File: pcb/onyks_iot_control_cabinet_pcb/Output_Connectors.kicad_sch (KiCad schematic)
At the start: 2 parts, among them J5 Conn_02x09_Odd_Even, J6 Conn_01x06_Socket

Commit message: Quick Fixes
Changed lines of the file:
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@@
 			(font
 				(size 3.81 3.81)
-				(thickness 0.762)
-				(bold yes)
+				(thickness 0.4763)
 			)
 		)
@@
 			(font
 				(size 3.81 3.81)
-				(thickness 0.762)
-				(bold yes)
+				(thickness 0.4763)
 			)
 		)

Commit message: Quick fixes
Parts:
- renumbered J5 to J8, J6 to J9
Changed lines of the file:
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@@
 		(dnp no)
 		(fields_autoplaced yes)
-		(property "Reference" "J6"
+		(property "Reference" "J9"
 			(at 163.83 76.2001 0)
 			(effects
@@
 			(project "onyks_iot_control_cabinet_pcb"
 				(path "/789878cb-67d5-4bc7-a42d-b3bc72d661d0/9fa608f4-5282-4caa-ae1b-46582b97cb5d"
-					(reference "J6")
+					(reference "J9")
 					(unit 1)
 				)
@@
 		(on_board yes)
 		(dnp no)
-		(property "Reference" "#PWR025"
+		(property "Reference" "#PWR033"
 			(at 149.86 72.39 0)
 			(effects
@@
 			(project "onyks_iot_control_cabinet_pcb"
 				(path "/789878cb-67d5-4bc7-a42d-b3bc72d661d0/9fa608f4-5282-4caa-ae1b-46582b97cb5d"
-					(reference "#PWR025")
+					(reference "#PWR033")
 					(unit 1)
 				)
@@
 		(dnp no)
 		(fields_autoplaced yes)
-		(property "Reference" "J5"
+		(property "Reference" "J8"
 			(at 153.67 104.14 0)
 			(effects
@@
 			(project "onyks_iot_control_cabinet_pcb"
 				(path "/789878cb-67d5-4bc7-a42d-b3bc72d661d0/9fa608f4-5282-4caa-ae1b-46582b97cb5d"
-					(reference "J5")
+					(reference "J8")
 					(unit 1)
 				)
@@
 		(dnp no)
 		(fields_autoplaced yes)
-		(property "Reference" "#PWR027"
+		(property "Reference" "#PWR035"
 			(at 162.56 139.7 0)
 			(effects
@@
 			(project "onyks_iot_control_cabinet_pcb"
 				(path "/789878cb-67d5-4bc7-a42d-b3bc72d661d0/9fa608f4-5282-4caa-ae1b-46582b97cb5d"
-					(reference "#PWR027")
+					(reference "#PWR035")
 					(unit 1)
 				)
@@
 		(on_board yes)
 		(dnp no)
-		(property "Reference" "#PWR026"
+		(property "Reference" "#PWR034"
 			(at 146.05 73.66 0)
 			(effects
@@
 			(project "onyks_iot_control_cabinet_pcb"
 				(path "/789878cb-67d5-4bc7-a42d-b3bc72d661d0/9fa608f4-5282-4caa-ae1b-46582b97cb5d"
-					(reference "#PWR026")
-					(unit 1)
-				)
+					(reference "#PWR034")
+					(unit 1)
+				)

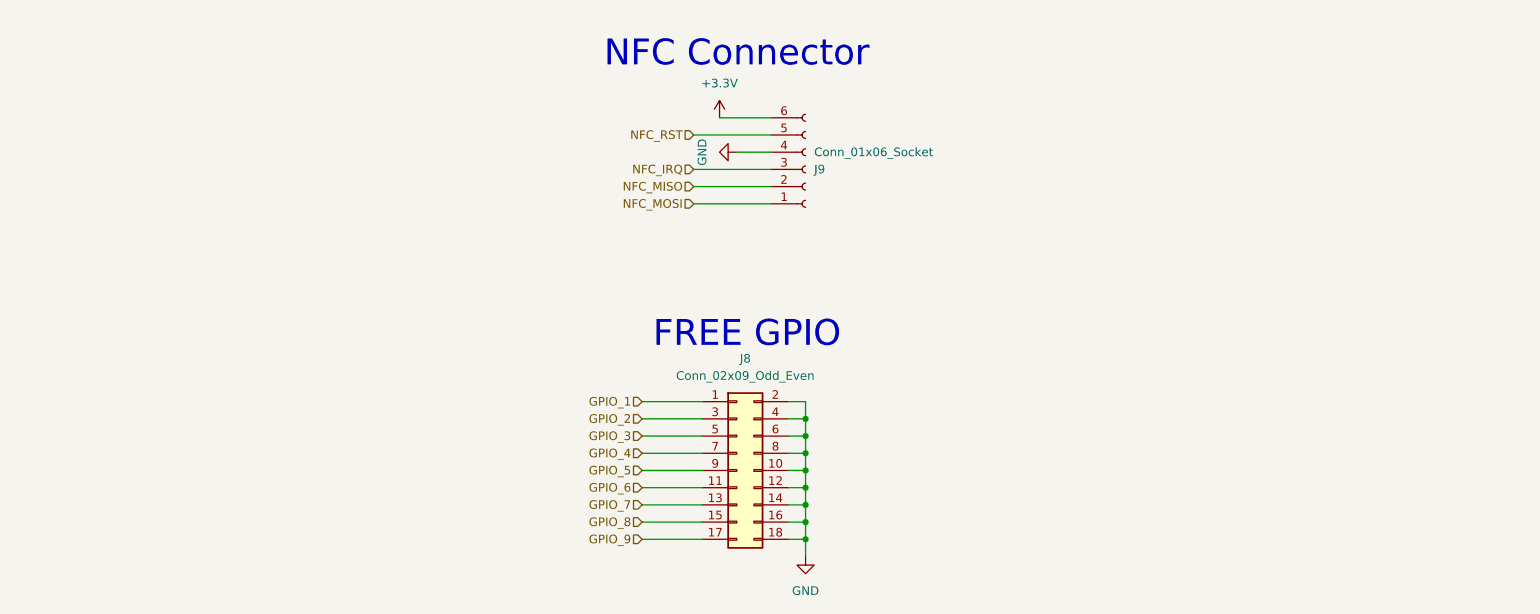
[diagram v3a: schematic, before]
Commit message: Update of the power supply and added the header for 125kHz RFID
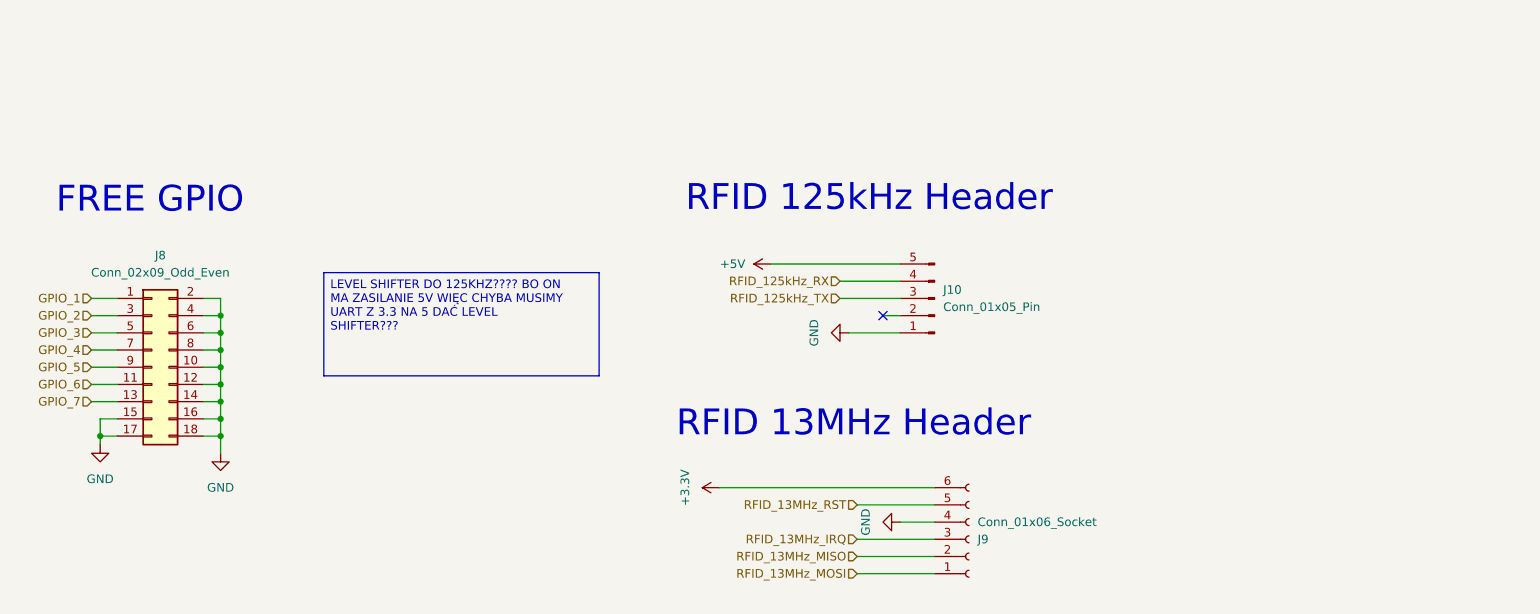
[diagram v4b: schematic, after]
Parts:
- added J10: Conn_01x05_Pin, symbol Connector:Conn_01x05_Pin
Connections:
- net GPIO_8 is gone; now on net GND: J8.15 (Pin_15)
- net GPIO_9 is gone; now on net GND: J8.17 (Pin_17)
- net GND: now also J10.1 (Pin_1)
- net NFC_IRQ renamed RFID_13MHz_IRQ
- net NFC_MISO renamed RFID_13MHz_MISO
- net NFC_MOSI renamed RFID_13MHz_MOSI
- net NFC_RST renamed RFID_13MHz_RST
- new net +5V: J10.5 (Pin_5)
- new net RFID_125kHz_RX: J10.4 (Pin_4)
- new net RFID_125kHz_TX: J10.3 (Pin_3)
- no-connect marks 0 -> 1
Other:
- note added: "RFID 125kHz Header"
- note added: "RFID 13MHz Header"
- note removed: "NFC Connector"
- company: (none) -> ,,Onyks'' Students Scientific Association
- title: (none) -> Onyks Iot Control Cabinet
- moved on the sheet: J8, J9

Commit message: Logic Shifter for RFID 125 KHz
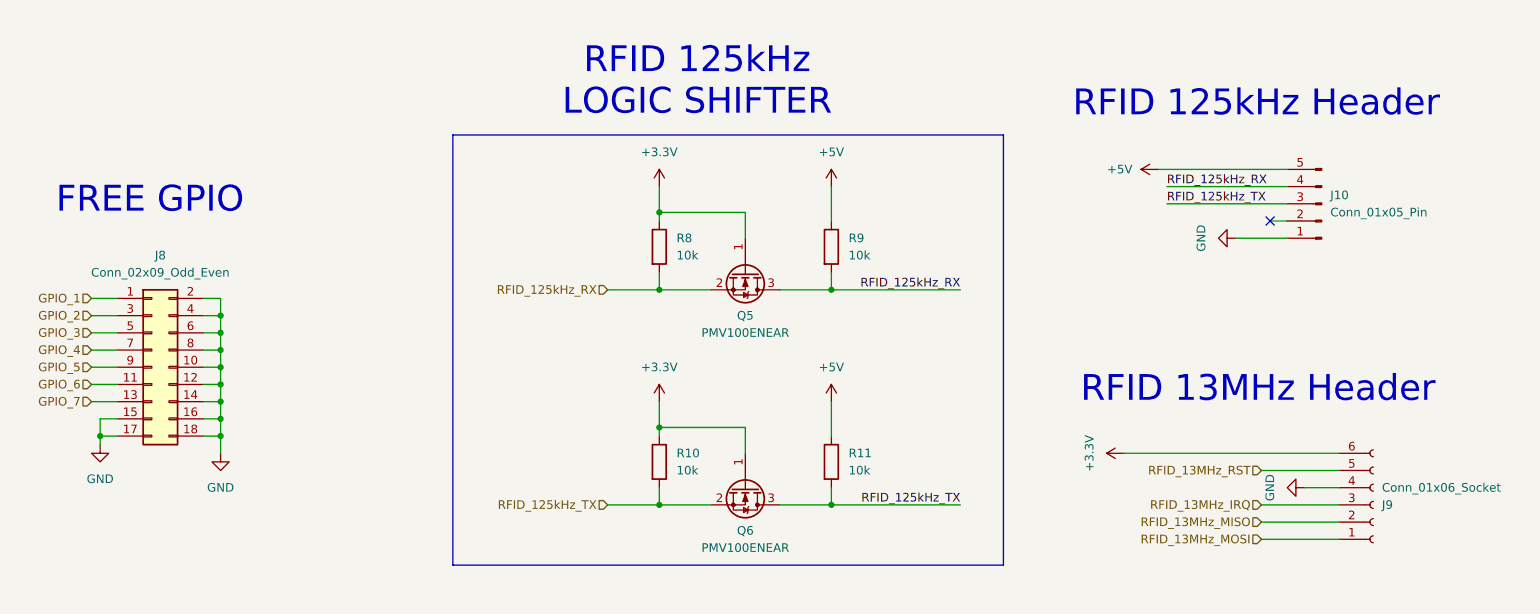
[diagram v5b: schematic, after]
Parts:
- added Q5, Q6: PMV100ENEAR, Package_TO_SOT_SMD:SOT-23, symbol Transistor_FET:2N7002
- added R10, R11, R8, R9: 10k, Resistor_SMD:R_0805_2012Metric_Pad1.20x1.40mm_HandSolder, symbol Device:R
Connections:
- net +3.3V: now also Q5.1 (G), Q6.1 (G), R10.1, R8.1
- net +5V: now also R11.1, R9.1
- net RFID_125kHz_RX: now also Q5.2 (S), Q5.3 (D), R8.2, R9.2
- net RFID_125kHz_TX: now also Q6.2 (S), Q6.3 (D), R10.2, R11.2
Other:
- note added: "RFID 125kHz LOGIC SHIFTER"
- moved on the sheet: J10, J9

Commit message: Schematics update; power supply and footprints fixes
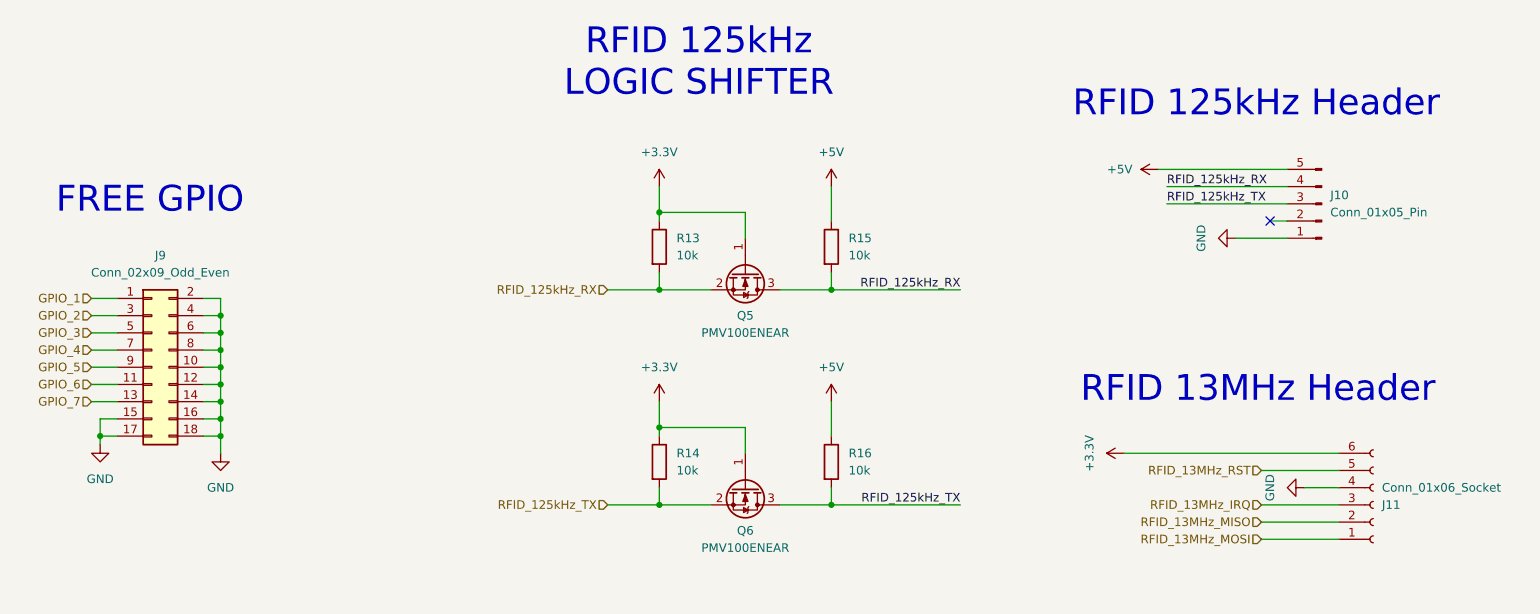
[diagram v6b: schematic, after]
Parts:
- J10: footprint (none) -> Connector_PinHeader_2.54mm:PinHeader_1x05_P2.54mm_Vertical
- renumbered J9 to J11, J8 to J9, R8 to R13, R10 to R14, R9 to R15, R11 to R16
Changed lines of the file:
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@@
 		(comment 2 "Jakub Jastrzębski")
 	)
-	(rectangle
-		(start 110.49 71.12)
-		(end 191.77 134.62)
-		(stroke
-			(width 0)
-			(type default)
-		)
-		(fill
-			(type none)
-		)
-	)
 	(text "RFID 125kHz \nLOGIC SHIFTER"
 		(exclude_from_sim no)
-		(at 146.558 63.246 0)
+		(at 146.812 60.452 0)
 		(effects
 			(font
@@
 		(dnp no)
 		(fields_autoplaced yes)
-		(property "Reference" "J9"
+		(property "Reference" "J11"
 			(at 247.65 125.7301 0)
 			(effects
@@
 			(project "onyks_iot_control_cabinet_pcb"
 				(path "/789878cb-67d5-4bc7-a42d-b3bc72d661d0/9fa608f4-5282-4caa-ae1b-46582b97cb5d"
-					(reference "J9")
+					(reference "J11")
 					(unit 1)
 				)
@@
 		(on_board yes)
 		(dnp no)
-		(property "Reference" "#PWR044"
+		(property "Reference" "#PWR050"
 			(at 140.97 114.3 0)
 			(effects
@@
 			(project "onyks_iot_control_cabinet_pcb"
 				(path "/789878cb-67d5-4bc7-a42d-b3bc72d661d0/9fa608f4-5282-4caa-ae1b-46582b97cb5d"
-					(reference "#PWR044")
+					(reference "#PWR050")
 					(unit 1)
 				)
@@
 		(dnp no)
 		(fields_autoplaced yes)
-		(property "Reference" "#PWR036"
+		(property "Reference" "#PWR051"
 			(at 166.37 82.55 0)
 			(effects
@@
 			(project "onyks_iot_control_cabinet_pcb"
 				(path "/789878cb-67d5-4bc7-a42d-b3bc72d661d0/9fa608f4-5282-4caa-ae1b-46582b97cb5d"
-					(reference "#PWR036")
+					(reference "#PWR051")
 					(unit 1)
 				)
@@
 		(on_board yes)
 		(dnp no)
-		(property "Reference" "#PWR033"
+		(property "Reference" "#PWR053"
 			(at 213.36 118.11 0)
 			(effects
@@
 			(project "onyks_iot_control_cabinet_pcb"
 				(path "/789878cb-67d5-4bc7-a42d-b3bc72d661d0/9fa608f4-5282-4caa-ae1b-46582b97cb5d"
-					(reference "#PWR033")
+					(reference "#PWR053")
 					(unit 1)
 				)
@@
 		(dnp no)
 		(fields_autoplaced yes)
-		(property "Reference" "#PWR045"
+		(property "Reference" "#PWR052"
 			(at 166.37 114.3 0)
 			(effects
@@
 			(project "onyks_iot_control_cabinet_pcb"
 				(path "/789878cb-67d5-4bc7-a42d-b3bc72d661d0/9fa608f4-5282-4caa-ae1b-46582b97cb5d"
-					(reference "#PWR045")
+					(reference "#PWR052")
 					(unit 1)
 				)
@@
 		(dnp no)
 		(fields_autoplaced yes)
-		(property "Reference" "J8"
+		(property "Reference" "J9"
 			(at 67.31 88.9 0)
 			(effects
@@
 			(project "onyks_iot_control_cabinet_pcb"
 				(path "/789878cb-67d5-4bc7-a42d-b3bc72d661d0/9fa608f4-5282-4caa-ae1b-46582b97cb5d"
-					(reference "J8")
+					(reference "J9")
 					(unit 1)
 				)
@@
 		(dnp no)
 		(fields_autoplaced yes)
-		(property "Reference" "#PWR021"
+		(property "Reference" "#PWR054"
 			(at 218.44 76.2 0)
 			(effects
@@
 			(project ""
 				(path "/789878cb-67d5-4bc7-a42d-b3bc72d661d0/9fa608f4-5282-4caa-ae1b-46582b97cb5d"
-					(reference "#PWR021")
+					(reference "#PWR054")
 					(unit 1)
 				)
@@
 		(dnp no)
 		(fields_autoplaced yes)
-		(property "Reference" "R8"
+		(property "Reference" "R13"
 			(at 143.51 86.3599 0)
 			(effects
@@
 			(project "onyks_iot_control_cabinet_pcb"
 				(path "/789878cb-67d5-4bc7-a42d-b3bc72d661d0/9fa608f4-5282-4caa-ae1b-46582b97cb5d"
-					(reference "R8")
+					(reference "R13")
 					(unit 1)
 				)
@@
 			)
 		)
-		(property "Footprint" ""
+		(property "Footprint" "Connector_PinHeader_2.54mm:PinHeader_1x05_P2.54mm_Vertical"
 			(at 238.76 81.28 0)
 			(effects
@@
 		(dnp no)
 		(fields_autoplaced yes)
-		(property "Reference" "#PWR023"
+		(property "Reference" "#PWR047"
 			(at 58.42 123.19 0)
 			(effects
@@
 			(project "onyks_iot_control_cabinet_pcb"
 				(path "/789878cb-67d5-4bc7-a42d-b3bc72d661d0/9fa608f4-5282-4caa-ae1b-46582b97cb5d"
-					(reference "#PWR023")
+					(reference "#PWR047")
 					(unit 1)
 				)
@@
 		(on_board yes)
 		(dnp no)
-		(property "Reference" "#PWR022"
+		(property "Reference" "#PWR055"
 			(at 219.71 86.36 0)
 			(effects
@@
 			(project "onyks_iot_control_cabinet_pcb"
 				(path "/789878cb-67d5-4bc7-a42d-b3bc72d661d0/9fa608f4-5282-4caa-ae1b-46582b97cb5d"
-					(reference "#PWR022")
+					(reference "#PWR055")
 					(unit 1)
 				)
@@
 		(dnp no)
 		(fields_autoplaced yes)
-		(property "Reference" "R10"
+		(property "Reference" "R14"
 			(at 143.51 118.1099 0)
 			(effects
@@
 			(project "onyks_iot_control_cabinet_pcb"
 				(path "/789878cb-67d5-4bc7-a42d-b3bc72d661d0/9fa608f4-5282-4caa-ae1b-46582b97cb5d"
-					(reference "R10")
+					(reference "R14")
 					(unit 1)
 				)
@@
 		(dnp no)
 		(fields_autoplaced yes)
-		(property "Reference" "R11"
+		(property "Reference" "R16"
 			(at 168.91 118.1099 0)
 			(effects
@@
 			(project "onyks_iot_control_cabinet_pcb"
 				(path "/789878cb-67d5-4bc7-a42d-b3bc72d661d0/9fa608f4-5282-4caa-ae1b-46582b97cb5d"
-					(reference "R11")
+					(reference "R16")
 					(unit 1)
 				)
@@
 		(dnp no)
 		(fields_autoplaced yes)
-		(property "Reference" "#PWR035"
+		(property "Reference" "#PWR048"
 			(at 76.2 124.46 0)
 			(effects
@@
 			(project "onyks_iot_control_cabinet_pcb"
 				(path "/789878cb-67d5-4bc7-a42d-b3bc72d661d0/9fa608f4-5282-4caa-ae1b-46582b97cb5d"
-					(reference "#PWR035")
+					(reference "#PWR048")
 					(unit 1)
 				)
@@
 		(on_board yes)
 		(dnp no)
-		(property "Reference" "#PWR034"
+		(property "Reference" "#PWR056"
 			(at 229.87 123.19 0)
 			(effects
@@
 			(project "onyks_iot_control_cabinet_pcb"
 				(path "/789878cb-67d5-4bc7-a42d-b3bc72d661d0/9fa608f4-5282-4caa-ae1b-46582b97cb5d"
-					(reference "#PWR034")
+					(reference "#PWR056")
 					(unit 1)
 				)
@@
 		(dnp no)
 		(fields_autoplaced yes)
-		(property "Reference" "R9"
+		(property "Reference" "R15"
 			(at 168.91 86.3599 0)
 			(effects
@@
 			(project "onyks_iot_control_cabinet_pcb"
 				(path "/789878cb-67d5-4bc7-a42d-b3bc72d661d0/9fa608f4-5282-4caa-ae1b-46582b97cb5d"
-					(reference "R9")
+					(reference "R15")
 					(unit 1)
 				)
@@
 		(on_board yes)
 		(dnp no)
-		(property "Reference" "#PWR024"
+		(property "Reference" "#PWR049"
 			(at 140.97 82.55 0)
 			(effects
@@
 			(project "onyks_iot_control_cabinet_pcb"
 				(path "/789878cb-67d5-4bc7-a42d-b3bc72d661d0/9fa608f4-5282-4caa-ae1b-46582b97cb5d"
-					(reference "#PWR024")
+					(reference "#PWR049")
 					(unit 1)
 				)

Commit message: PCB Ressurection
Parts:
- R13, R14, R15, R16: value 10k -> 10k/5%

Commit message: PCB Update
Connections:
- net GPIO_1 renamed GPIO_O1
- net GPIO_2 renamed GPIO_O2
- net GPIO_3 renamed GPIO_O3
- net GPIO_4 renamed GPIO_O4
- net GPIO_5 renamed GPIO_O5
- net GPIO_6 renamed GPIO_O6
- net GPIO_7 renamed GPIO_O7
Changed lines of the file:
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@@
 		)
 	)
-	(hierarchical_label "GPIO_2"
+	(hierarchical_label "GPIO_O2"
 		(shape input)
 		(at 57.15 97.79 180)
@@
 		)
 	)
-	(hierarchical_label "GPIO_4"
+	(hierarchical_label "GPIO_O4"
 		(shape input)
 		(at 57.15 102.87 180)
@@
 		)
 	)
-	(hierarchical_label "GPIO_6"
+	(hierarchical_label "GPIO_O6"
 		(shape input)
 		(at 57.15 107.95 180)
@@
 		)
 	)
-	(hierarchical_label "GPIO_3"
+	(hierarchical_label "GPIO_O3"
 		(shape input)
 		(at 57.15 100.33 180)
@@
 		)
 	)
-	(hierarchical_label "GPIO_1"
+	(hierarchical_label "GPIO_O1"
 		(shape input)
 		(at 57.15 95.25 180)
@@
 		)
 	)
-	(hierarchical_label "GPIO_7"
+	(hierarchical_label "GPIO_O7"
 		(shape input)
 		(at 57.15 110.49 180)
@@
 		)
 	)
-	(hierarchical_label "GPIO_5"
+	(hierarchical_label "GPIO_O5"
 		(shape input)
 		(at 57.15 105.41 180)
